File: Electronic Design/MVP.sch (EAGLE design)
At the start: 38 parts, among them IC1 ACS711KLCTR-12AB-T, IC3 ATMEGA328-PU, Q2 16MHz, Q3 IRF9540, Q4 IRF9540

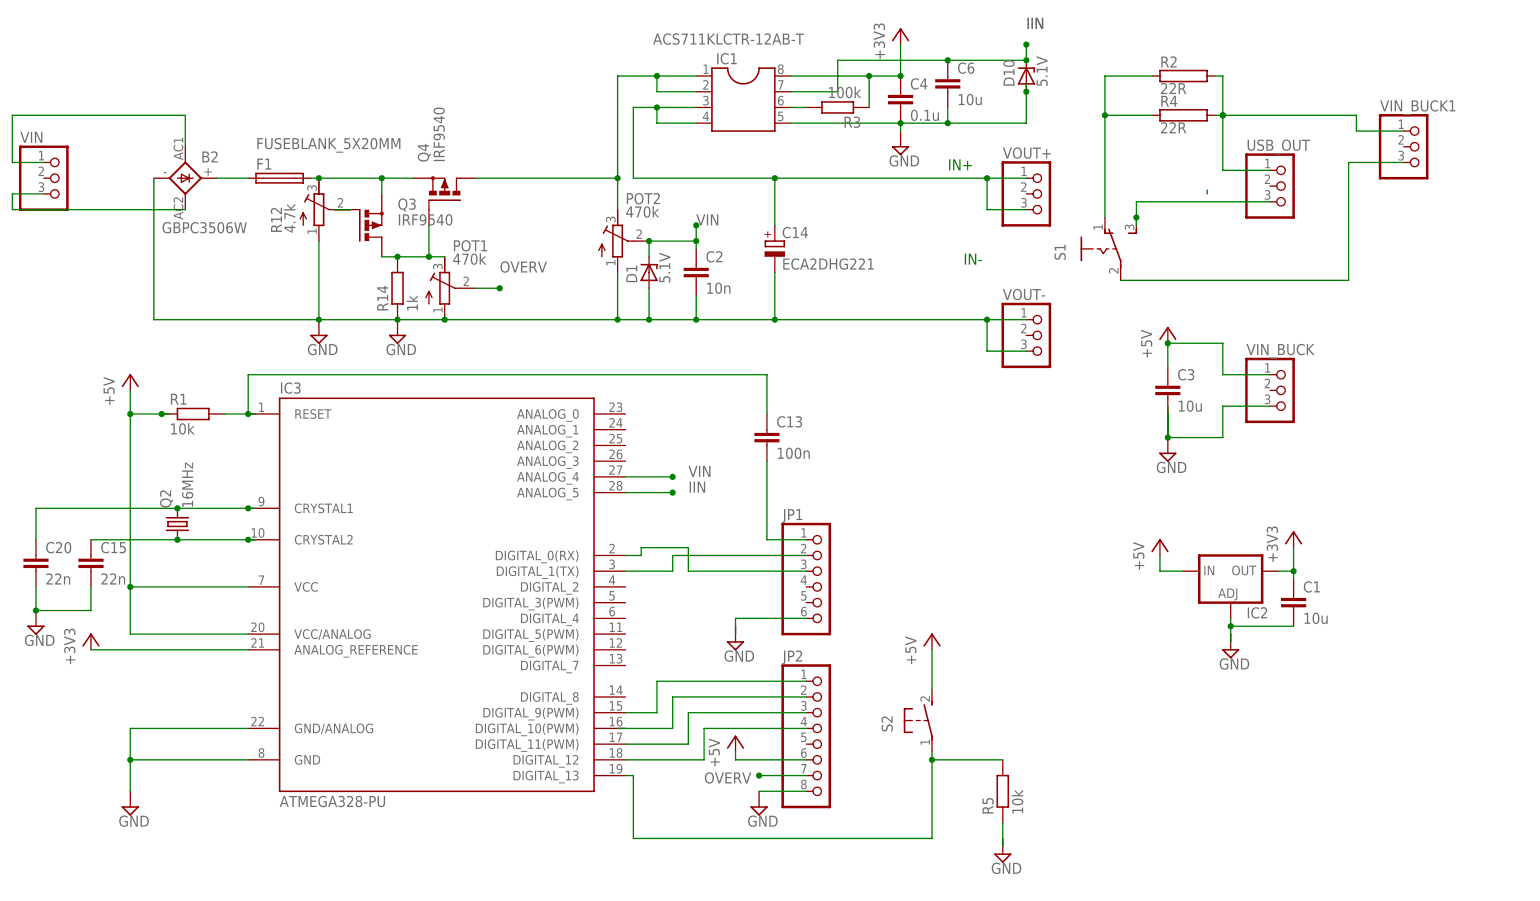
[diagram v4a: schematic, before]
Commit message: moved components into intial places on PCB
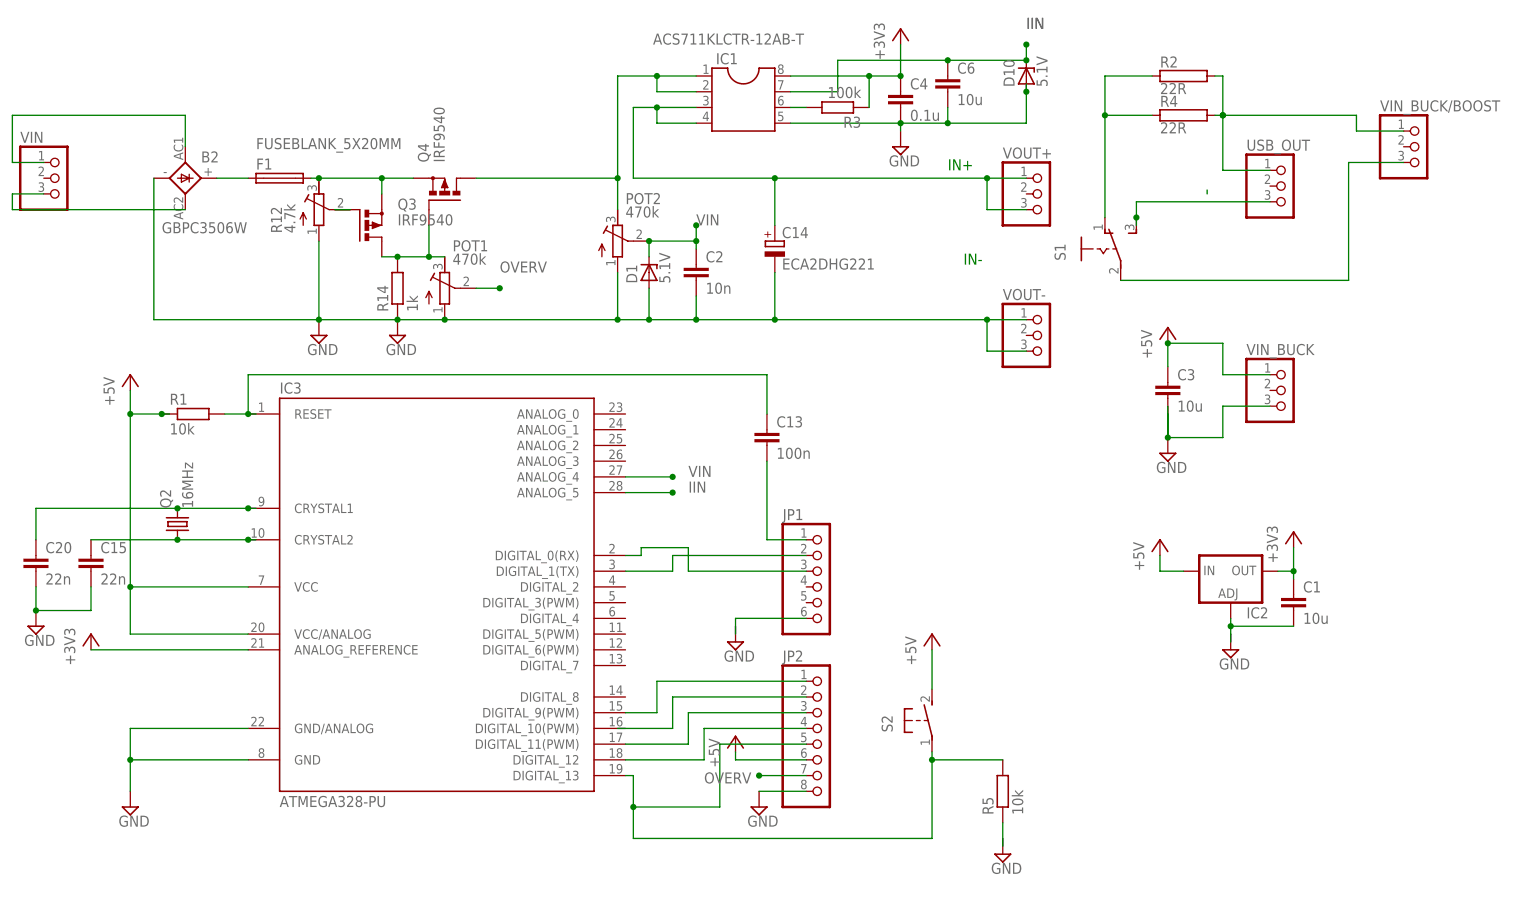
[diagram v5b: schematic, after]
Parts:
- renumbered VIN_BUCK1 to VIN_BUCK/BOOST
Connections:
- net N$8: now also JP2.5
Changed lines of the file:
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@@
 <part name="SUPPLY6" library="supply2" deviceset="GND" device=""/>
 <part name="C3" library="resistor" deviceset="C-EU" device="C1210" value="10u"/>
-<part name="VIN_BUCK1" library="pinhead" deviceset="PINHD-1X3" device=""/>
+<part name="VIN_BUCK/BOOST" library="pinhead" deviceset="PINHD-1X3" device=""/>
 <part name="R2" library="resistor-power" deviceset="R" device="RWM8X45" value="22R"/>
 <part name="R4" library="resistor-power" deviceset="R" device="RWM8X45" value="22R"/>
@@
 <instance part="SUPPLY6" gate="GND" x="5.08" y="13.97"/>
 <instance part="C3" gate="G$1" x="74.93" y="55.88"/>
-<instance part="VIN_BUCK1" gate="A" x="115.57" y="93.98"/>
+<instance part="VIN_BUCK/BOOST" gate="A" x="115.57" y="93.98"/>
 <instance part="R2" gate="G$1" x="77.47" y="105.41"/>
 <instance part="R4" gate="G$1" x="77.47" y="99.06"/>
@@
 <pinref part="IC3" gate="1" pin="DIGITAL_13"/>
 <wire x1="-12.7" y1="-7.62" x2="-11.43" y2="-7.62" width="0.1524" layer="91"/>
-<wire x1="-11.43" y1="-7.62" x2="-11.43" y2="-17.78" width="0.1524" layer="91"/>
+<wire x1="-11.43" y1="-7.62" x2="-11.43" y2="-12.7" width="0.1524" layer="91"/>
 <pinref part="S2" gate="1" pin="P"/>
+<wire x1="-11.43" y1="-12.7" x2="-11.43" y2="-17.78" width="0.1524" layer="91"/>
 <wire x1="-11.43" y1="-17.78" x2="36.83" y2="-17.78" width="0.1524" layer="91"/>
 <wire x1="36.83" y1="-17.78" x2="36.83" y2="-5.08" width="0.1524" layer="91"/>
@@
 <wire x1="48.26" y1="-5.08" x2="36.83" y2="-5.08" width="0.1524" layer="91"/>
 <junction x="36.83" y="-5.08"/>
+<wire x1="2.54" y1="-2.54" x2="2.54" y2="-12.7" width="0.1524" layer="91"/>
+<wire x1="2.54" y1="-12.7" x2="-11.43" y2="-12.7" width="0.1524" layer="91"/>
+<junction x="-11.43" y="-12.7"/>
+<pinref part="JP2" gate="A" pin="5"/>
+<wire x1="16.51" y1="-2.54" x2="2.54" y2="-2.54" width="0.1524" layer="91"/>
 </segment>
 </net>
@@
 <wire x1="67.31" y1="72.39" x2="104.14" y2="72.39" width="0.1524" layer="91"/>
 <wire x1="104.14" y1="72.39" x2="104.14" y2="91.44" width="0.1524" layer="91"/>
-<pinref part="VIN_BUCK1" gate="A" pin="3"/>
+<pinref part="VIN_BUCK/BOOST" gate="A" pin="3"/>
 <wire x1="113.03" y1="91.44" x2="104.14" y2="91.44" width="0.1524" layer="91"/>
 </segment>
@@
 <junction x="83.82" y="99.06"/>
 <junction x="83.82" y="99.06"/>
-<pinref part="VIN_BUCK1" gate="A" pin="1"/>
+<pinref part="VIN_BUCK/BOOST" gate="A" pin="1"/>
 <wire x1="113.03" y1="96.52" x2="105.41" y2="96.52" width="0.1524" layer="91"/>
 <wire x1="105.41" y1="96.52" x2="105.41" y2="99.06" width="0.1524" layer="91"/>

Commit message: First pass at adding traces
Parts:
- S2: device switch-omron:31-XX -> switch-omron:10-XX
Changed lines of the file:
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@@
 <setting verticaltext="up"/>
 </settings>
-<grid distance="0.05" unitdist="inch" unit="inch" style="lines" multiple="1" display="no" altdistance="0.01" altunitdist="inch" altunit="inch"/>
+<grid distance="0.1" unitdist="inch" unit="inch" style="lines" multiple="1" display="no" altdistance="0.01" altunitdist="inch" altunit="inch"/>
 <layers>
 <layer number="1" name="Top" color="4" fill="1" visible="no" active="no"/>
@@
 <part name="S1" library="switch" deviceset="255SB" device=""/>
 <part name="USB_OUT" library="pinhead" deviceset="PINHD-1X3" device=""/>
-<part name="S2" library="switch-omron" deviceset="31-XX" device=""/>
+<part name="S2" library="switch-omron" deviceset="10-XX" device=""/>
 <part name="+5V2" library="supply1" deviceset="+5V" device=""/>
 <part name="R5" library="resistor" deviceset="R-EU_" device="R1210" value="10k"/>

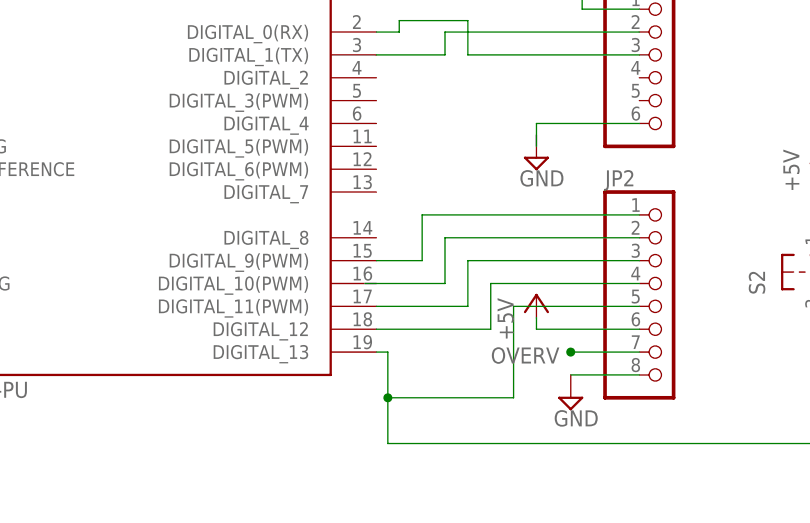
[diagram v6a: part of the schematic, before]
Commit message: adding trace for pin16 on atmega to go to jumper
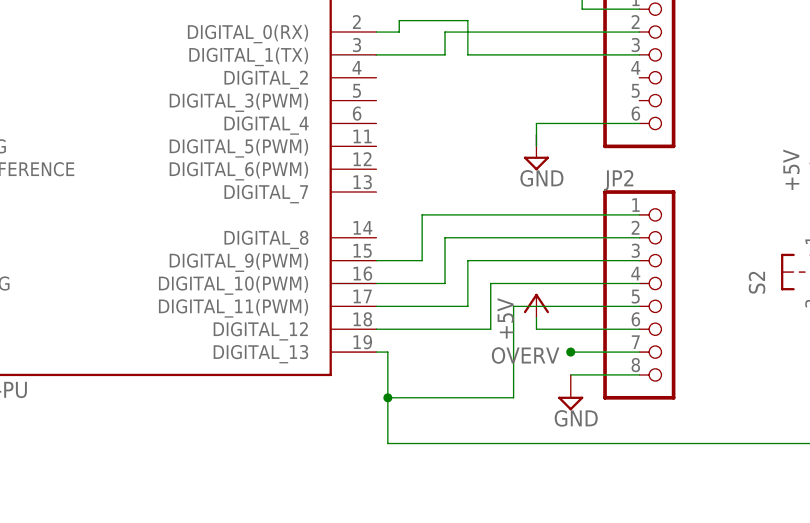
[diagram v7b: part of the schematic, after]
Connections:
- net N$9: now also IC3.DIGITAL_10(PWM)
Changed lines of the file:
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@@
 <wire x1="16.51" y1="5.08" x2="-5.08" y2="5.08" width="0.1524" layer="91"/>
 <wire x1="-5.08" y1="5.08" x2="-5.08" y2="0" width="0.1524" layer="91"/>
-<wire x1="-5.08" y1="0" x2="-13.97" y2="0" width="0.1524" layer="91"/>
+<pinref part="IC3" gate="1" pin="DIGITAL_10(PWM)"/>
+<wire x1="-5.08" y1="0" x2="-12.7" y2="0" width="0.1524" layer="91"/>
 </segment>
 </net>
